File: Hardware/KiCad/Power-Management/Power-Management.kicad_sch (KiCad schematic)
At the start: 51 parts, among them IC1 RT9080-33GJ5, J1 Screw_Terminal_01x02, J2 Conn_01x06, J3 Screw_Terminal_01x02, K1 FINDER-36.11, Q1 BC817, T1 ZMPT101B, U1 STM32F401CCU6, U2 ACS758xCB-050B-PFF, U3 ESP-01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

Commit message: feat: project libraries
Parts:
- removed F1: Fuse, Fuse:Fuseholder_Clip-5x20mm_Keystone_3512P_Inline_P23.62x7.27mm_D1.02x2.41x1.02x1.57mm_Horizontal, symbol Device:Fuse
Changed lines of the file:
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@@
-	)
-	(symbol
-		(lib_id "Device:Fuse")
-		(at 69.85 63.5 0)
-		(unit 1)
-		(exclude_from_sim no)
-		(in_bom yes)
-		(on_board yes)
-		(dnp no)
-		(fields_autoplaced yes)
-		(property "Reference" "F1"
-			(at 72.39 62.2299 0)
-			(effects
-				(font
-					(size 1.27 1.27)
-				)
-				(justify left)
-			)
-		)
-		(property "Value" "Fuse"
-			(at 72.39 64.7699 0)
-			(effects
-				(font
-					(size 1.27 1.27)
-				)
-				(justify left)
-			)
-		)
-		(property "Footprint" "Fuse:Fuseholder_Clip-5x20mm_Keystone_3512P_Inline_P23.62x7.27mm_D1.02x2.41x1.02x1.57mm_Horizontal"
-			(at 68.072 63.5 90)
-			(effects
-				(font
-					(size 1.27 1.27)
-				)
-				(hide yes)
-			)
-		)
-		(property "Datasheet" "~"
-			(at 69.85 63.5 0)
-			(effects
-				(font
-					(size 1.27 1.27)
-				)
-				(hide yes)
-			)
-		)
-		(property "Description" "Fuse"
-			(at 69.85 63.5 0)
-			(effects
-				(font
-					(size 1.27 1.27)
-				)
-				(hide yes)
-			)
-		)
-		(pin "1"
-		)
-		(pin "2"
-		)
-		(instances
-			(project ""
-				(path "/8164d6a1-c4f4-44c7-a4ee-8f3e33b11c0e"
-					(reference "F1")
-					(unit 1)
-				)
-			)
-		)
 	)
 	(symbol

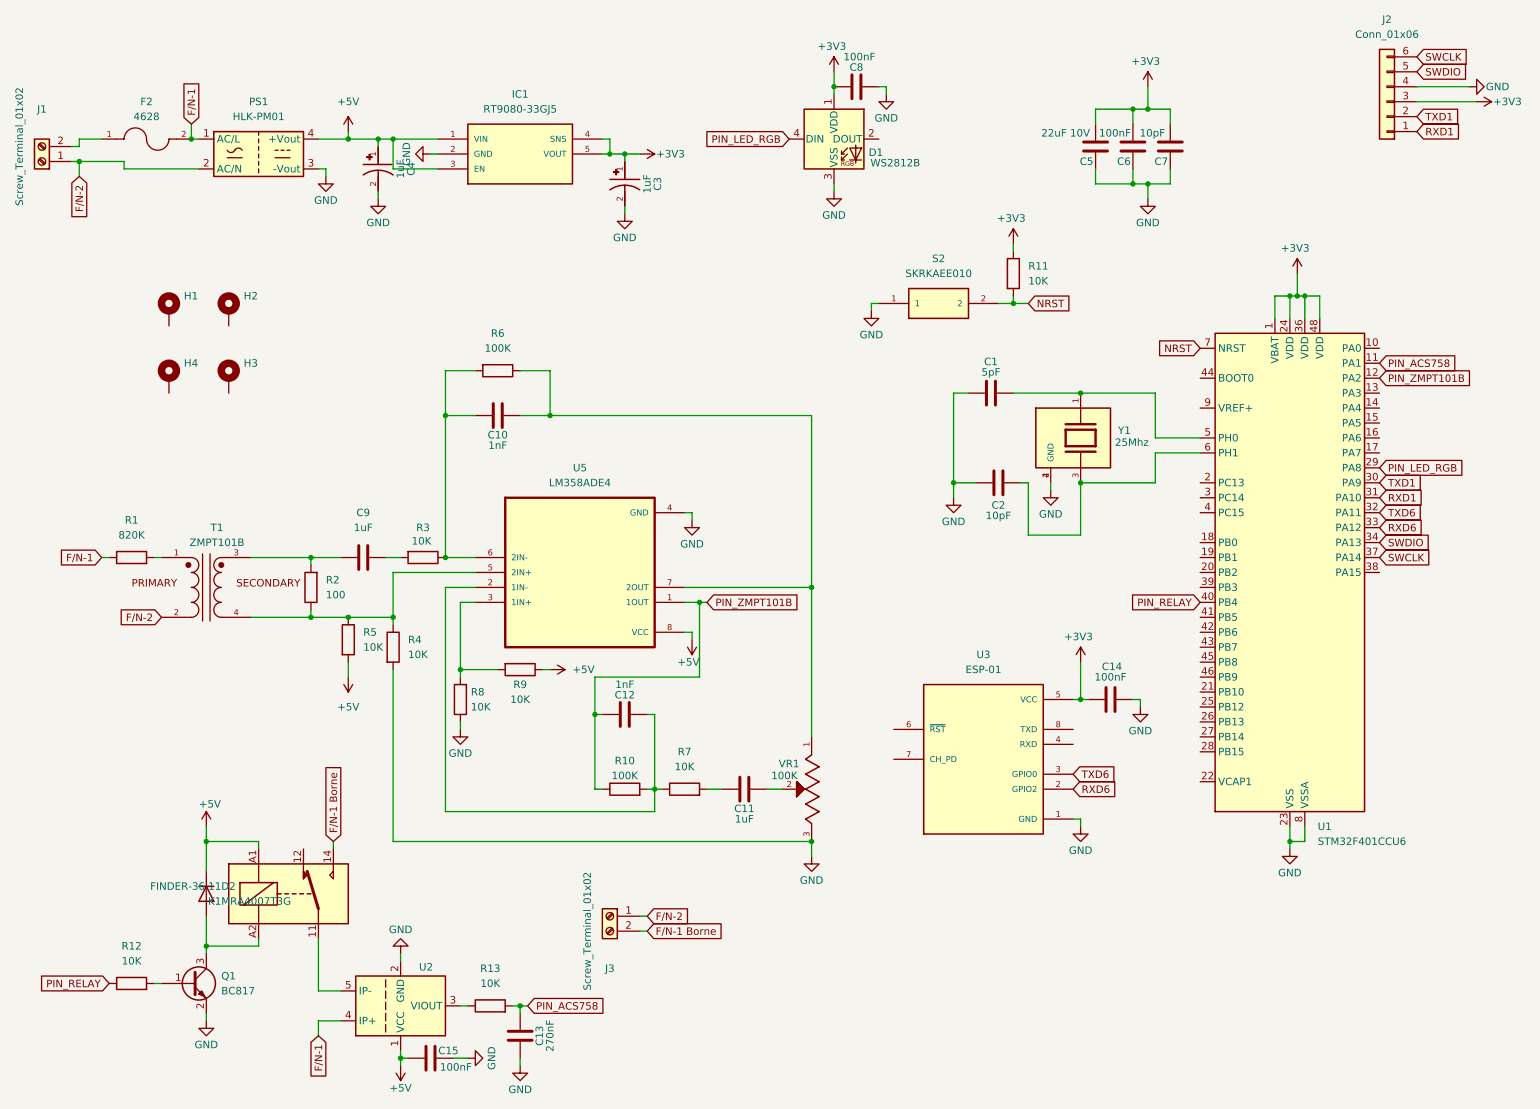
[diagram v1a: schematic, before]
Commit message: feat: hierarchical sheet
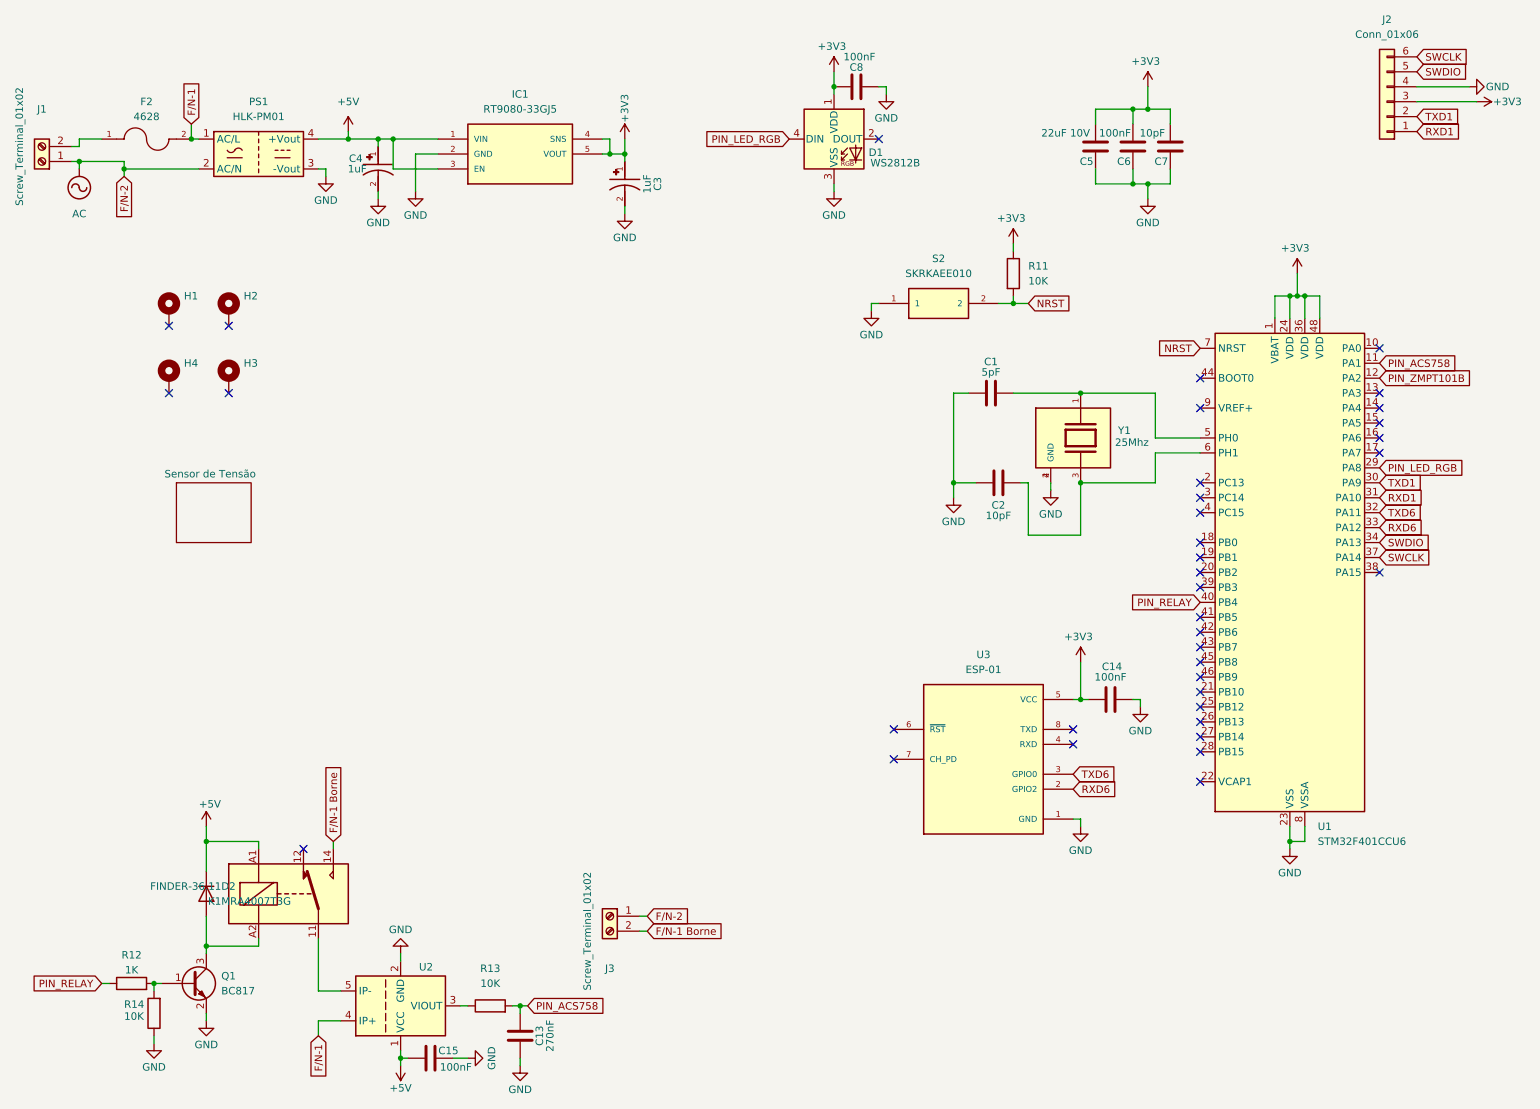
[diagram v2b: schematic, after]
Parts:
- removed C10, C12: 1nF, Capacitor_SMD:C_0805_2012Metric_Pad1.18x1.45mm_HandSolder, symbol Device:C
- removed C11, C9: 1uF, Capacitor_SMD:C_0805_2012Metric_Pad1.18x1.45mm_HandSolder, symbol Device:C
- removed R1: 820K, Resistor_SMD:R_0805_2012Metric_Pad1.20x1.40mm_HandSolder, symbol Device:R
- removed R10, R6: 100K, Resistor_SMD:R_0805_2012Metric_Pad1.20x1.40mm_HandSolder, symbol Device:R
- removed R2: 100, Resistor_SMD:R_0805_2012Metric_Pad1.20x1.40mm_HandSolder, symbol Device:R
- removed R3, R4, R5, R7, R8, R9: 10K, Resistor_SMD:R_0805_2012Metric_Pad1.20x1.40mm_HandSolder, symbol Device:R
- removed T1: ZMPT101B, ZMPT101B:XFMR_ZMPT101B, symbol ZMPT101B:ZMPT101B
- removed U5: LM358ADE4, LM358ADE4:SOIC127P599X175-8N, symbol LM358ADE4:LM358ADE4
- removed VR1: 100K, 3296W-OT1-103LF:TRIM_3296W-OT1-103LF, symbol 3296W-OT1-103LF:3296W-OT1-103LF
- added R14: 10K, Resistor_SMD:R_0805_2012Metric_Pad1.20x1.40mm_HandSolder, symbol Device:R
- R12: value 10K -> 1K
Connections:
- net GND: now also R14.1
- net at Q1.1 (B), R12.2: now also R14.2
- net F/N-2 renamed AC
- no-connect marks 0 -> 37
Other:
- added sheet Sensor de Tensão (untitled.kicad_sch)
- title: Schematic Power Manegement -> Power Manegement
